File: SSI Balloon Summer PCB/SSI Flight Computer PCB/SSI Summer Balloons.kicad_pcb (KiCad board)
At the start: 4 copper layers, 77.5 x 61 mm, 101 parts, among them J1 Battery connector, J2 Conn_01x02, J3 LoRa antenna, J6 1040310811, J7 GPS antenna, J8 PT1000 Sensor, J9 Camera, M1 MountingHole_3.2mm_M3, M2 MountingHole_3.2mm_M3, M3 MountingHole_3.2mm_M3, M4 MountingHole_3.2mm_M3, Q2 DMG2305UX-7, SW1 NRST, SW2 BOOT0, U1 RFM95W-915S2, U10 MS5611-01BA03, U11 TPS63070RNMR, U3 AP2112K-3.3TRG1, U4 ICM-42688-P, U7 STM32F411CEUx, U8 MAX-M10S-00B, U9 MAX31865ATP_T, Y1 ABM8W-12.0000MHZ-8-K1Z-T3

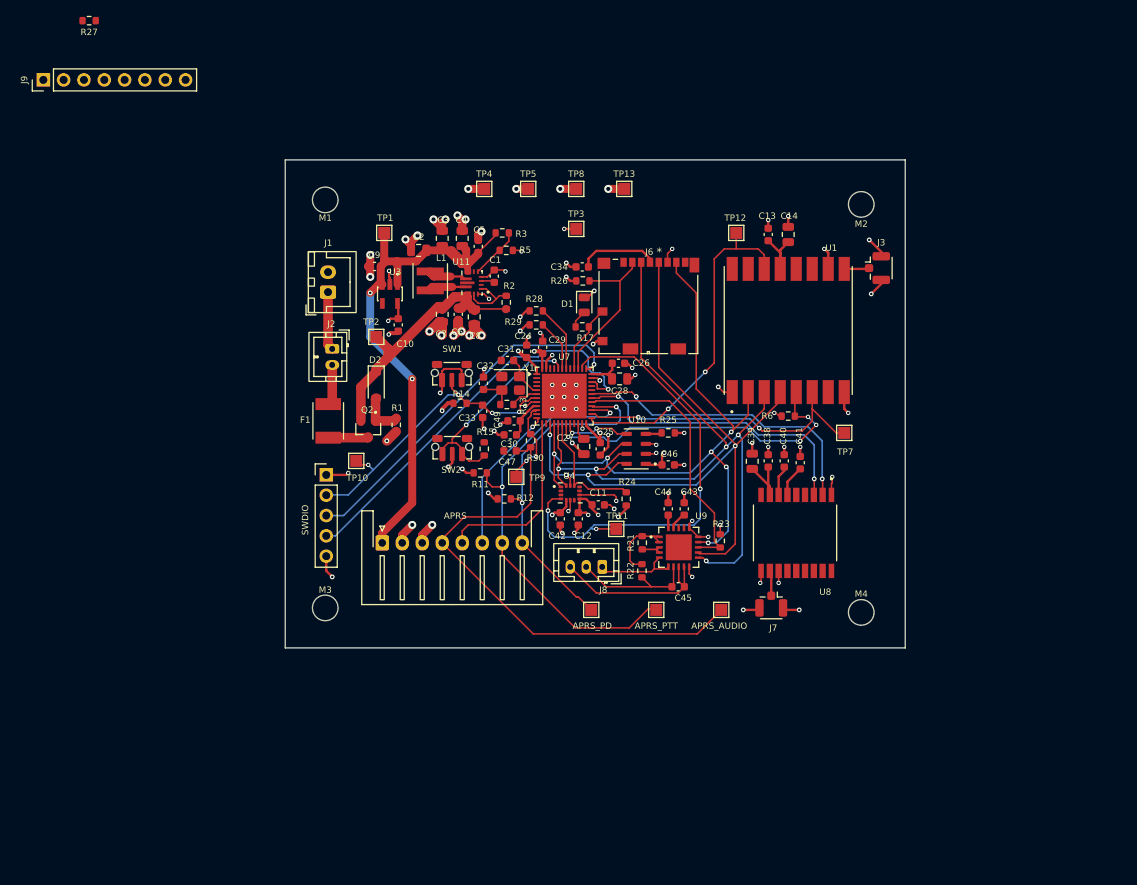
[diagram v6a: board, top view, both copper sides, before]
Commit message: Added Headers for testing, finalizing PCB
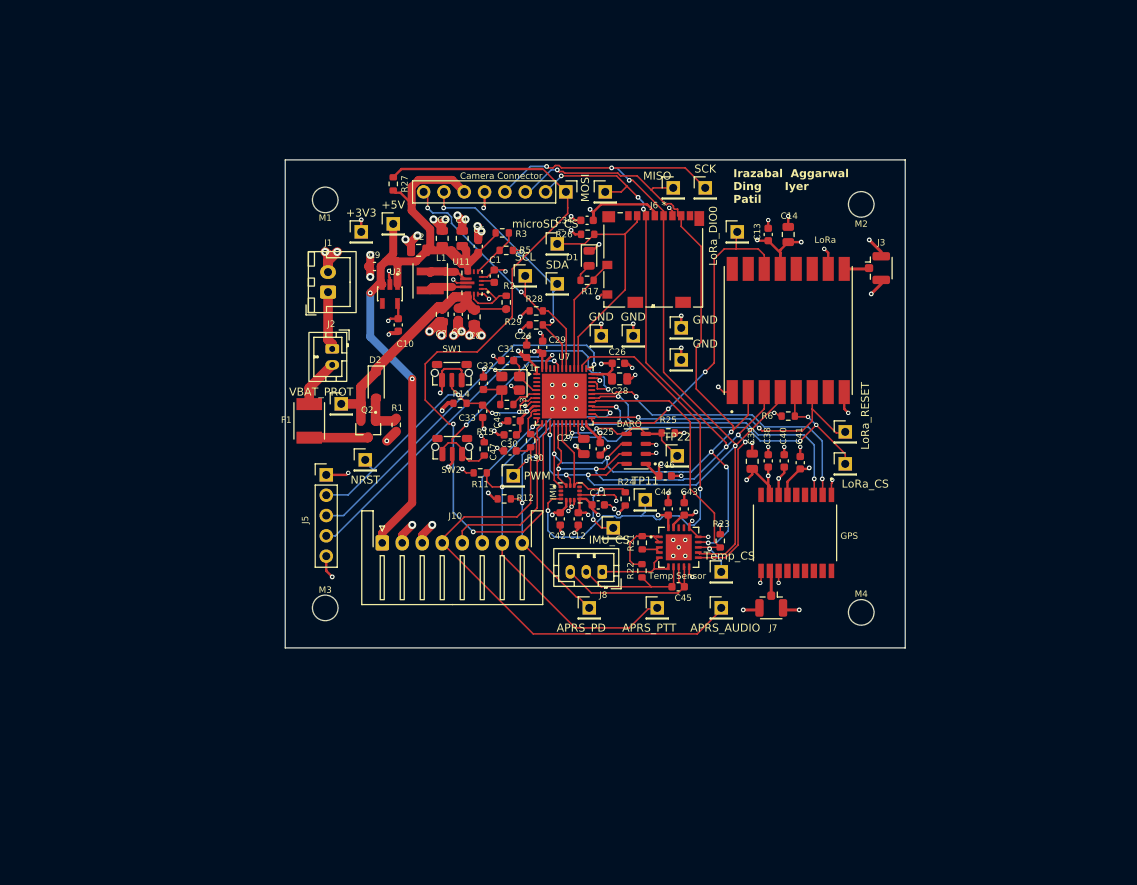
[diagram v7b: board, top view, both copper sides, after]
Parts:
- removed the APRS_AUDIO at (154.5, 132.8)
- removed the APRS_PD at (138.2, 132.8)
- removed the APRS_PTT at (146.4, 132.8)
- removed TP1, TP10, TP12, TP13, TP2, TP3, TP4, TP5, TP7, TP8, TP9: TestPoint, TestPoint:TestPoint_Pad_1.5x1.5mm
- added +3V3: Conn_01x01, Connector_PinHeader_2.54mm:PinHeader_1x01_P2.54mm_Vertical, F.Cu at (109.5, 85.5)
- added +5V: Conn_01x01, Connector_PinHeader_2.54mm:PinHeader_1x01_P2.54mm_Vertical, F.Cu at (113.5, 84.5)
- added APRS_AUDIO: Conn_01x01, Connector_PinHeader_2.54mm:PinHeader_1x01_P2.54mm_Vertical, F.Cu at (154.5, 132.5)
- added APRS_PD: Conn_01x01, Connector_PinHeader_2.54mm:PinHeader_1x01_P2.54mm_Vertical, F.Cu at (138.0, 132.5)
- added APRS_PTT: Conn_01x01, Connector_PinHeader_2.54mm:PinHeader_1x01_P2.54mm_Vertical, F.Cu at (146.5, 132.5)
- added GND: Conn_01x01, Connector_PinHeader_2.54mm:PinHeader_1x01_P2.54mm_Vertical, F.Cu at (149.5, 101.5)
- added GND: Conn_01x01, Connector_PinHeader_2.54mm:PinHeader_1x01_P2.54mm_Vertical, F.Cu at (149.5, 97.5)
- added GND: Conn_01x01, Connector_PinHeader_2.54mm:PinHeader_1x01_P2.54mm_Vertical, F.Cu at (143.5, 98.5)
- added GND: Conn_01x01, Connector_PinHeader_2.54mm:PinHeader_1x01_P2.54mm_Vertical, F.Cu at (139.5, 98.5)
- added IMU_CS: Conn_01x01, Connector_PinHeader_2.54mm:PinHeader_1x01_P2.54mm_Vertical, F.Cu at (141.0, 122.5)
- added LoRa_CS: Conn_01x01, Connector_PinHeader_2.54mm:PinHeader_1x01_P2.54mm_Vertical, F.Cu at (170.0, 114.5)
- added LoRa_DIO0: Conn_01x01, Connector_PinHeader_2.54mm:PinHeader_1x01_P2.54mm_Vertical, F.Cu at (156.5, 85.5)
- added LoRa_RESET: Conn_01x01, Connector_PinHeader_2.54mm:PinHeader_1x01_P2.54mm_Vertical, F.Cu at (170.0, 110.5)
- added MISO: Conn_01x01, Connector_PinHeader_2.54mm:PinHeader_1x01_P2.54mm_Vertical, F.Cu at (148.5, 80.0)
- added MOSI: Conn_01x01, Connector_PinHeader_2.54mm:PinHeader_1x01_P2.54mm_Vertical, F.Cu at (140.0, 80.5)
- added NRST: Conn_01x01, Connector_PinHeader_2.54mm:PinHeader_1x01_P2.54mm_Vertical, F.Cu at (110.0, 114.0)
- added PWM: Conn_01x01, Connector_PinHeader_2.54mm:PinHeader_1x01_P2.54mm_Vertical, F.Cu at (128.5, 116.0)
- added SCK: Conn_01x01, Connector_PinHeader_2.54mm:PinHeader_1x01_P2.54mm_Vertical, F.Cu at (152.5, 80.0)
- added SCL: Conn_01x01, Connector_PinHeader_2.54mm:PinHeader_1x01_P2.54mm_Vertical, F.Cu at (130.0, 91.0)
- added SDA: Conn_01x01, Connector_PinHeader_2.54mm:PinHeader_1x01_P2.54mm_Vertical, F.Cu at (134.0, 92.0)
- added TP22: Conn_01x01, Connector_PinHeader_2.54mm:PinHeader_1x01_P2.54mm_Vertical, F.Cu at (149.0, 113.5)
- added Temp_CS: Conn_01x01, Connector_PinHeader_2.54mm:PinHeader_1x01_P2.54mm_Vertical, F.Cu at (154.5, 128.0)
- added VBAT_PROT: Conn_01x01, Connector_PinHeader_2.54mm:PinHeader_1x01_P2.54mm_Vertical, F.Cu at (107.0, 107.0)
- added microSD_CS: Conn_01x01, Connector_PinHeader_2.54mm:PinHeader_1x01_P2.54mm_Vertical, F.Cu at (134.0, 87.0)
- Camera Connector: renamed from J9
- TP11: value TestPoint -> Conn_01x01; footprint TestPoint:TestPoint_Pad_1.5x1.5mm -> Connector_PinHeader_2.54mm:PinHeader_1x01_P2.54mm_Vertical
- Temp Sensor: renamed from U9
- moved Camera Connector 66.8 mm to (135.1, 80.5), turned to -90 degrees
- moved R27 43.1 mm to (113.5, 79.5), turned to -90 degrees
- moved R26 5.85 mm to (137.8, 85.8)
- moved C34 5.85 mm to (137.7, 84.1)
- moved D1 5.85 mm to (138.0, 88.8)
- moved J6 5.85 mm to (146.0, 89.0)
- moved R17 5.85 mm to (137.7, 91.6)
- moved TP11 5.13 mm to (145.0, 119.0)
- moved F1 2.38 mm to (103.0, 109.1)
- moved C46 1.43 mm to (147.5, 116.0)
- moved J8 0.62 mm to (139.6, 128.0)
- moved R24 0.12 mm to (142.5, 118.9)
- renumbered U10 to BARO, U8 to GPS, U4 to IMU, APRS to J10, SWDIO to J5, U1 to LoRa
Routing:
- net /MCU (STM)/Cam_CS: track 0.00 -> 99.8 mm, vias 0 -> 2
- net /MCU (STM)/SCK: track 92.5 -> 135.1 mm, vias 4 -> 7
- net /MCU (STM)/MISO: track 83.1 -> 115.8 mm, vias 6 -> 7
- net /MCU (STM)/SDA: track 6.47 -> 35.2 mm, vias 0 -> 2
- net /MCU (STM)/SCL: track 8.42 -> 34.2 mm, vias 0 -> 2
- net /MCU (STM)/MOSI: track 94.2 -> 118.2 mm, vias 5 -> 8
- net +5V: track 71.2 -> 92.3 mm
- net GND: track 151.2 -> 169.7 mm, vias 84 -> 100
- net /MCU (STM)/microSD_CS: track 19.9 -> 31.2 mm
- net +3V3: track 98.3 -> 109.2 mm, vias 22 -> 33
- net /MCU (STM)/IMU_CS: track 15.5 -> 22.7 mm, vias 0 -> 2
- net /MCU (STM)/BARO_CS: track 10.6 -> 17.3 mm
- net /MCU (STM)/LoRa_CS: track 41.2 -> 47.6 mm
- net /MCU (STM)/microSD_detect: track 8.60 -> 14.5 mm
- net /MCU (STM)/Temp_CS: track 33.6 -> 37.3 mm, vias 0 -> 1
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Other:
- board text added: "Irazabal Aggarwal Ding Iyer Patil"

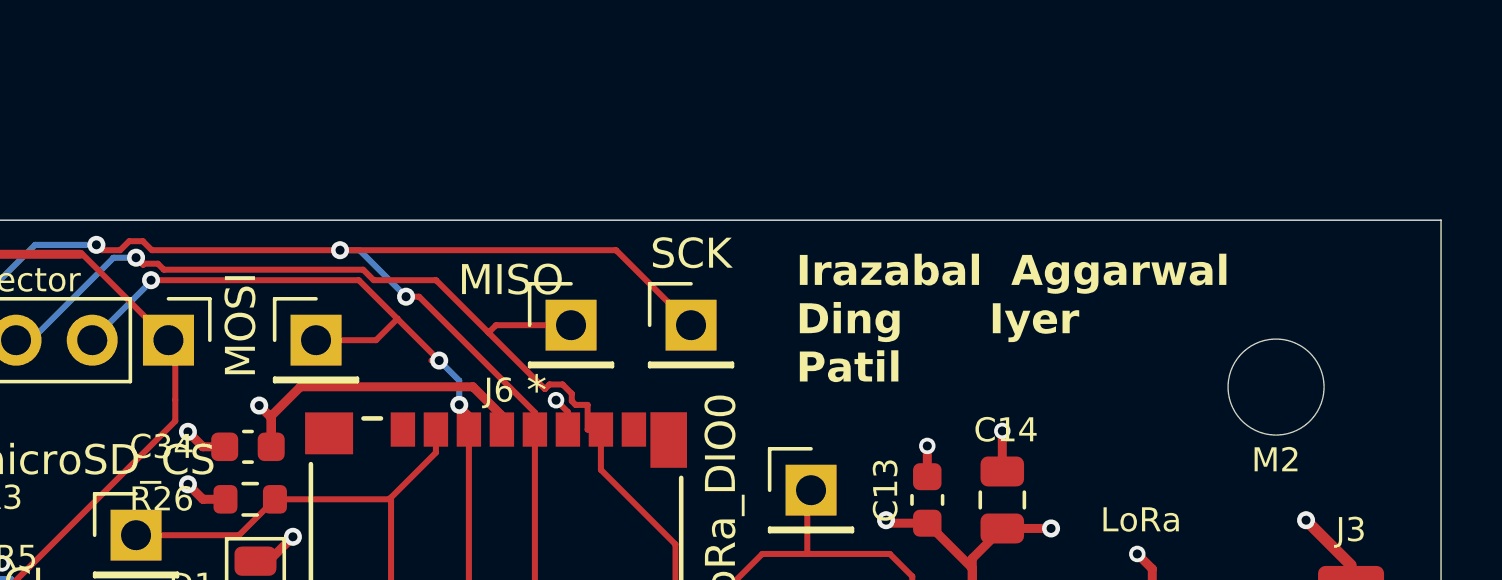
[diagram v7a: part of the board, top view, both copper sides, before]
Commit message: moved two pins for SD card
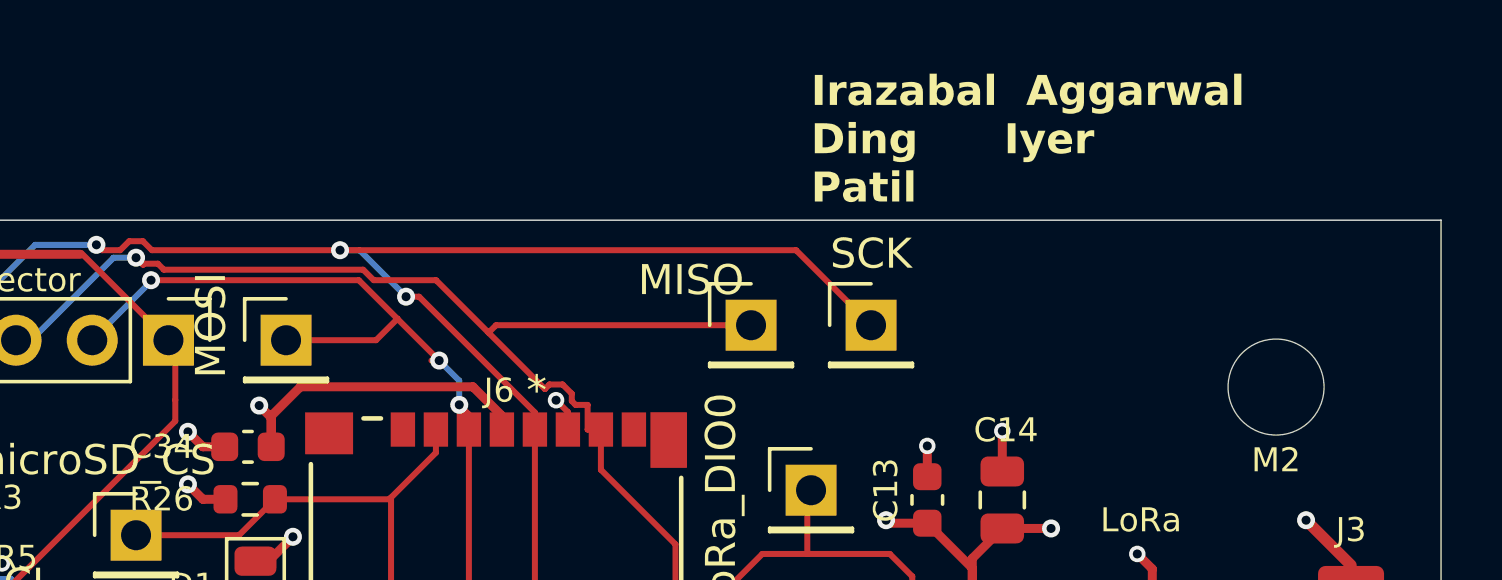
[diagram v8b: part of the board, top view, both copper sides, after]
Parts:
- moved MISO 6.00 mm to (154.5, 80.0)
- moved SCK 6.00 mm to (158.5, 80.0)
- moved MOSI 1.00 mm to (139.0, 80.5)
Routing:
- net /MCU (STM)/SCK: track 135.1 -> 141.1 mm
- net /MCU (STM)/MISO: track 115.8 -> 121.8 mm
- net /MCU (STM)/MOSI: track 118.2 -> 119.2 mm
